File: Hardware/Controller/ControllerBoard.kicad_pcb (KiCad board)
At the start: 2 copper layers, 25 x 140 mm, 31 parts, among them J1 Conn_01x08_MountingPin, J2 USB4715-GF-A_REVA, Q1 BC818, Q2 AO3401A, Q3 BC818, X1 CON_JST_PH_2PIN_MTPH2, X2 CON_JST_PH_2PIN_MTPH2

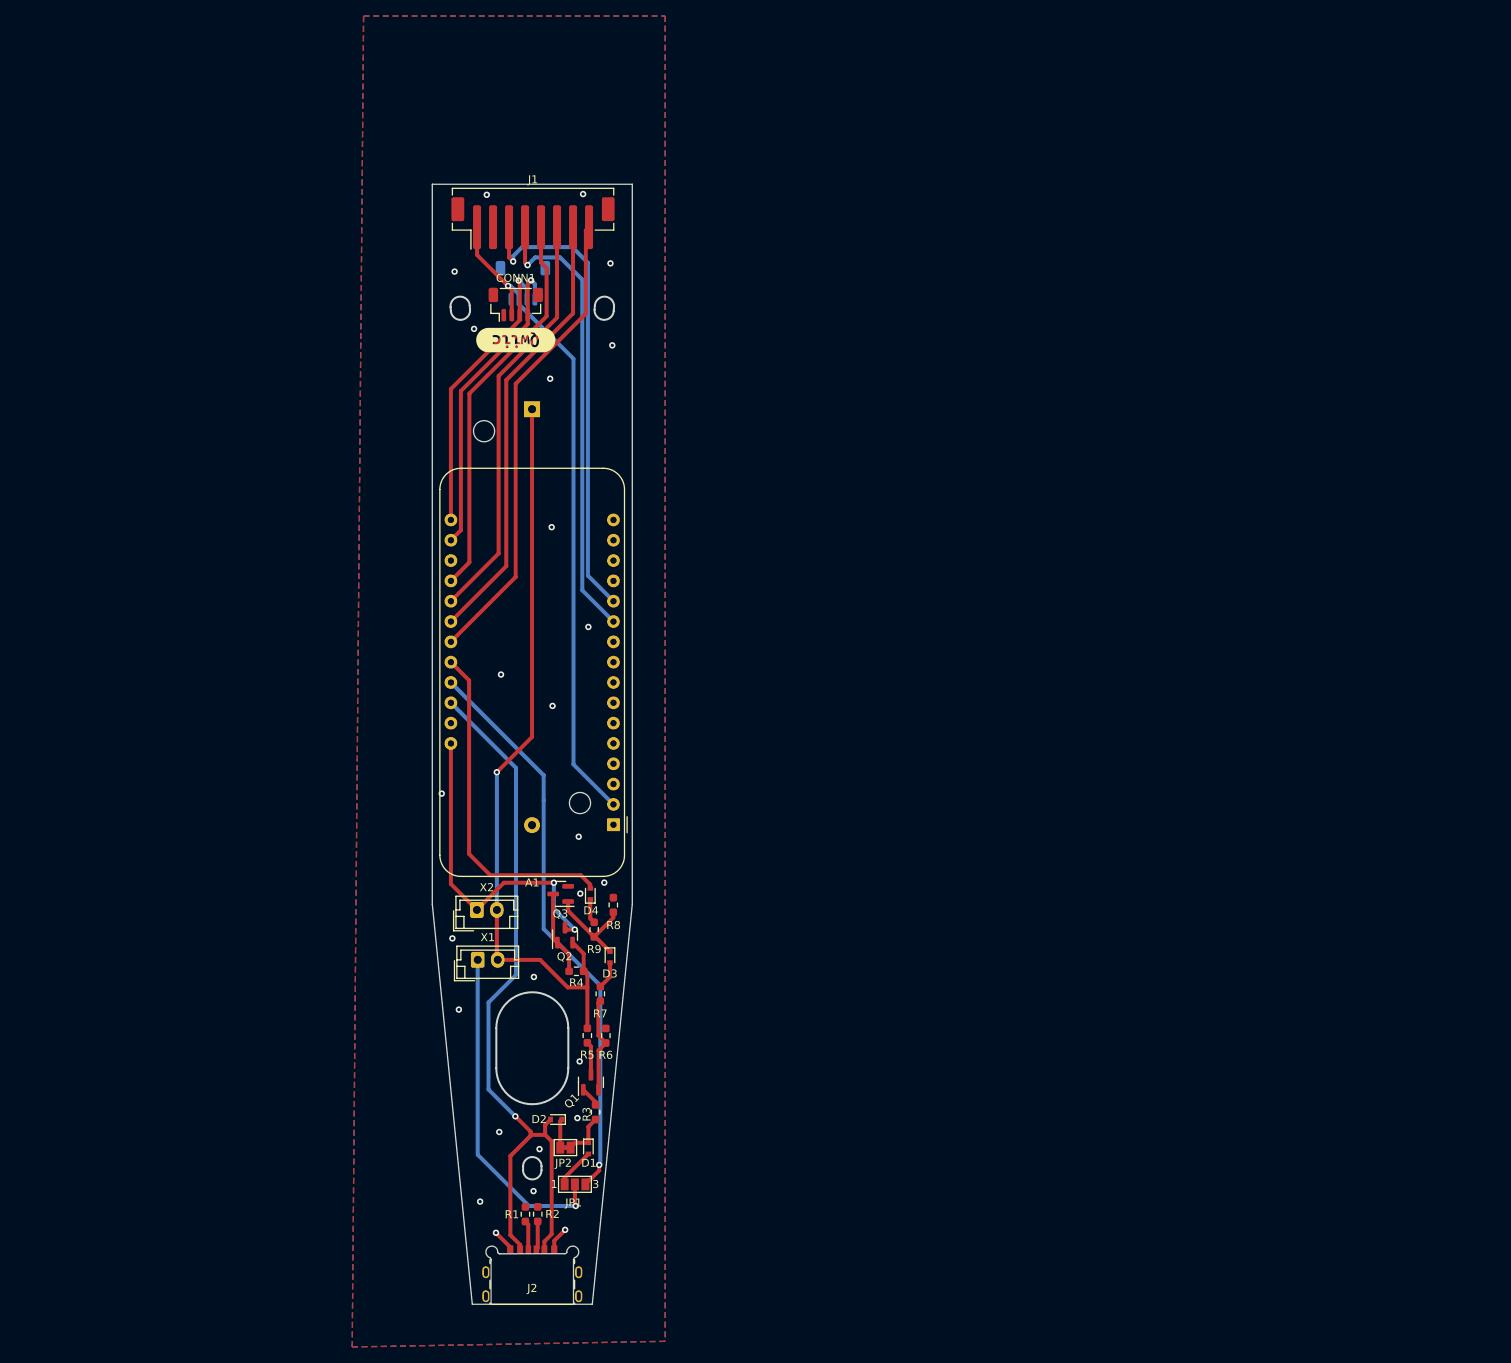
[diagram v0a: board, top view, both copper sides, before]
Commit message: Initial conversion and cleanup from a feather to an esp32s3
added USB power
Added switching 3.6-5v regulator
updated schematic ground to use built in kicad libraries
updated partially broken library references to eagle lib files
added circuit simulator of trigger and wakeup simulation

Signed-off-by: lokimetasmith <lokimail@gmail.com>
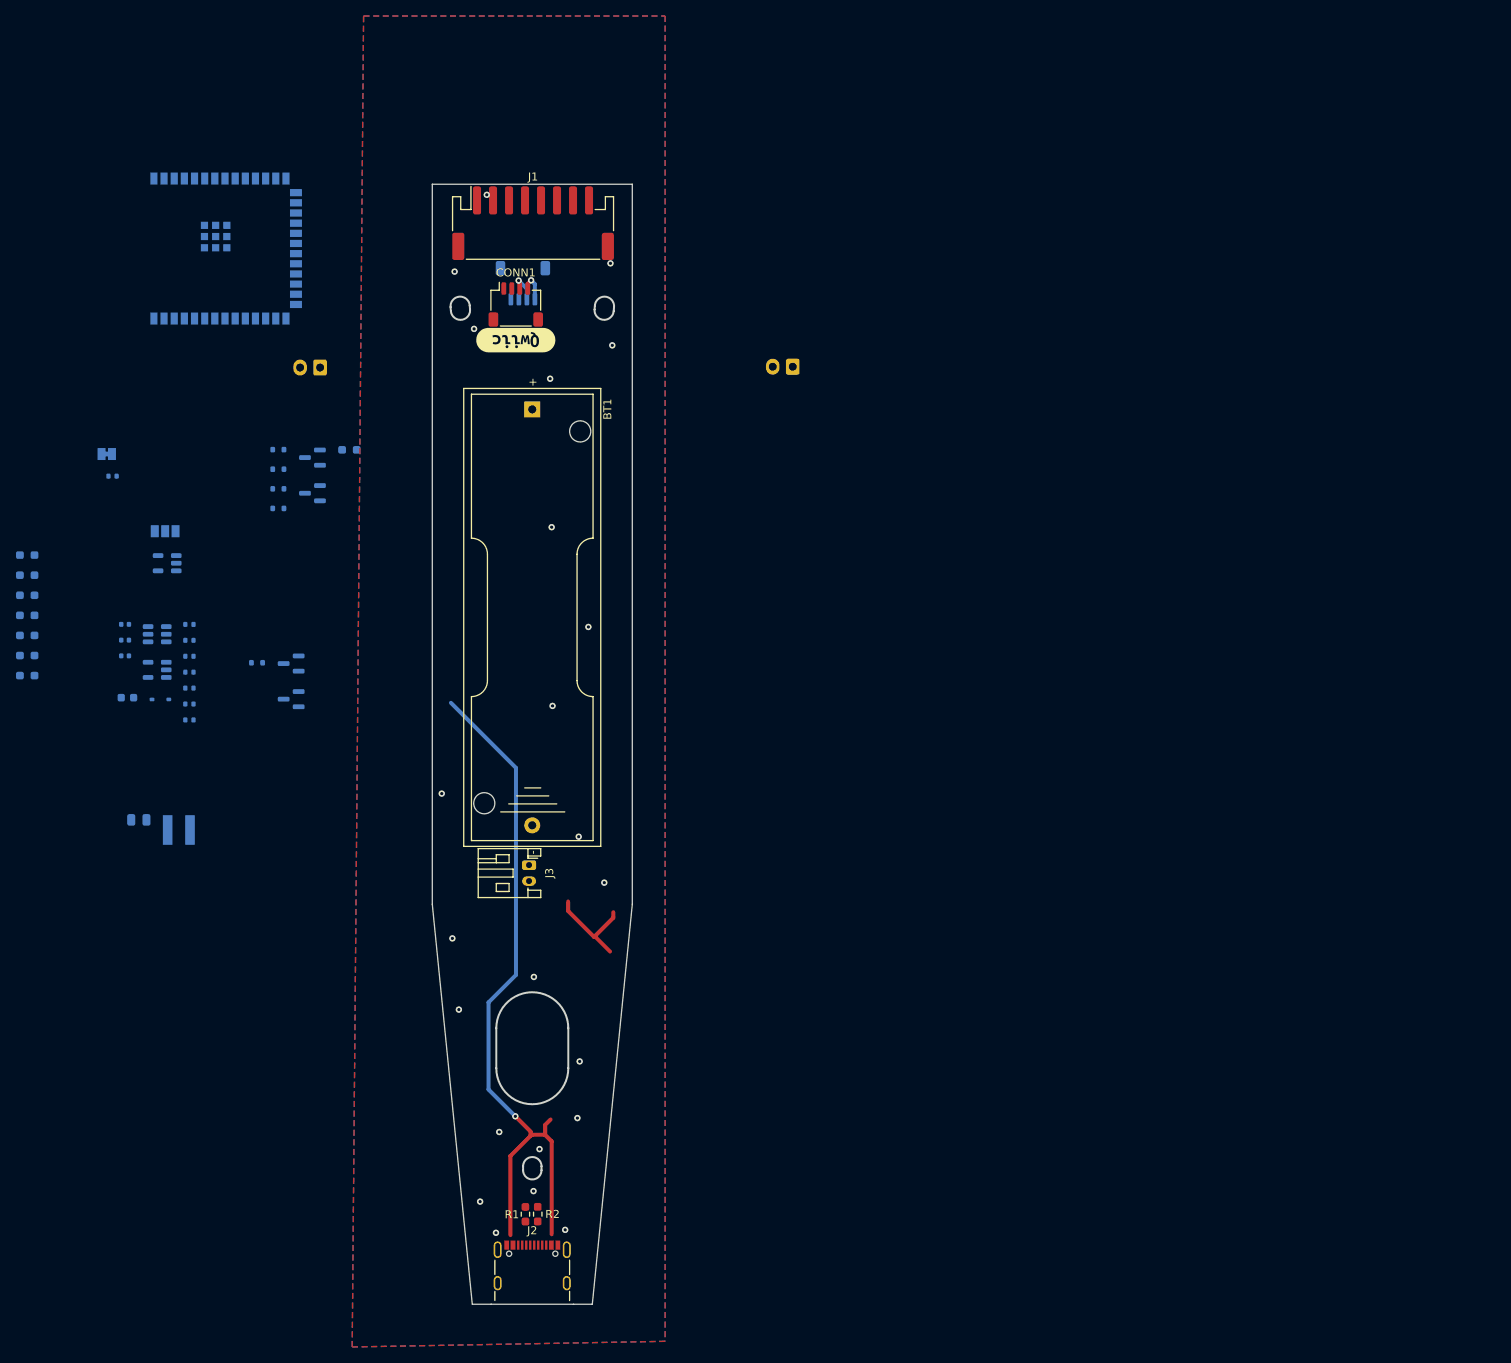
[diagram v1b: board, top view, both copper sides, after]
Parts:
- removed A1: Adafruit_Feather_HUZZAH32_ESP32, Module:Adafruit_Feather
- added C1: 2u, Capacitor_SMD:C_0603_1608Metric, B.Cu at (60.0, 99.2)
- added C2: 4.7u, Capacitor_SMD:C_0805_2012Metric, B.Cu at (61.5, 114.5)
- added C5: 6.8p, Capacitor_SMD:C_0402_1005Metric, B.Cu at (59.7, 90.0)
- added C6: 0.01u, Capacitor_SMD:C_0402_1005Metric, B.Cu at (59.7, 92.0)
- added C8: 0.1u, Capacitor_SMD:C_0402_1005Metric, B.Cu at (59.7, 94.0)
- added D5: 3.3v_TVS, Diode_SMD:D_SOD-323, B.Cu at (64.2, 99.4)
- added D6: BAS516, Diode_SMD:D_SOD-523, B.Cu at (76.2, 94.8)
- added J3: Conn_01x02_Male, Connector_JST:JST_PH_S2B-PH-K_1x02_P2.00mm_Horizontal, F.Cu at (110.2, 120.1)
- added L1: 2.2uH, Inductor_SMD:L_Taiyo-Yuden_MD-4040, B.Cu at (66.5, 115.7)
- added Q4: AO3401A, Package_TO_SOT_SMD:SOT-23, B.Cu at (80.5, 99.4)
- added R10: 15K, Resistor_SMD:R_0402_1005Metric, B.Cu at (67.8, 90.0)
- added R11: 15K, Resistor_SMD:R_0402_1005Metric, B.Cu at (67.8, 92.0)
- added R12: 27, Resistor_SMD:R_0402_1005Metric, B.Cu at (67.8, 94.0)
- added R13: 27, Resistor_SMD:R_0402_1005Metric, B.Cu at (67.8, 96.0)
- added R14: 10K, Resistor_SMD:R_0402_1005Metric, B.Cu at (67.8, 98.0)
- added R15: 680k, Resistor_SMD:R_0402_1005Metric, B.Cu at (67.8, 100.0)
- added R16: 150K, Resistor_SMD:R_0402_1005Metric, B.Cu at (67.8, 102.0)
- added R17: 5.1k, Resistor_SMD:R_0402_1005Metric, B.Cu at (58.2, 71.5)
- added R18: 100k, Resistor_SMD:R_0603_1608Metric_Pad0.98x0.95mm_HandSolder, B.Cu at (47.5, 96.4)
- added U1: ESP32-S3-WROOM-1, Espressif:ESP32-S3-WROOM-1, B.Cu at (71.6, 43.0)
- added U2: SN65220, Package_TO_SOT_SMD:SOT-23-6, B.Cu at (63.8, 91.3)
- added U3: TLV62569DBV, Package_TO_SOT_SMD:SOT-23-5, B.Cu at (63.8, 95.7)
- added U5: MCP73811T-420I-OT, Package_TO_SOT_SMD:SOT-23-5, B.Cu at (65.0, 82.4)
- BT1: moved to F.Cu
- CONN1: footprint Connector_JST:JST_SH_BM04B-SRSS-TB_1x04-1MP_P1.00mm_Vertical -> Connector_JST:JST_SH_SM04B-SRSS-TB_1x04-1MP_P1.00mm_Horizontal
- D1, D2, D3, D4, JP1, JP2, Q1, Q2, Q3, R3, R4, R5, R6, R7, R8, R9, X1, X2: moved to B.Cu
- J1: footprint Connector_JST:JST_PH_B8B-PH-SM4-TB_1x08-1MP_P2.00mm_Vertical -> Connector_JST:JST_PH_S8B-PH-SM4-TB_1x08-1MP_P2.00mm_Horizontal
- J2: value USB4715-GF-A_REVA -> USB_C_Receptacle_USB2.0; footprint USB4715-GF-A_REVA:GCT_USB4715-GF-A_REVA -> Connector_USB:USB_C_Receptacle_GCT_USB4105-xx-A_16P_TopMnt_Horizontal
- moved JP2 103.9 mm to (57.5, 68.7), turned to 180 degrees
- moved JP1 96.4 mm to (64.8, 78.4), turned to 180 degrees
- moved D1 95.6 mm to (78.9, 68.2), turned to 180 degrees
- moved R6 90.9 mm to (47.5, 86.4), turned to 180 degrees
- moved R5 90.6 mm to (47.5, 83.9), turned to 180 degrees
- moved D2 88.4 mm to (78.9, 70.6)
- moved R3 88.3 mm to (87.8, 68.2), turned to 180 degrees
- moved R4 86.1 mm to (47.5, 81.4)
- moved R7 85.9 mm to (47.5, 88.9), turned to 180 degrees
- moved Q1 85.5 mm to (83.2, 69.2), turned to 180 degrees
- moved X1 83.9 mm to (143.2, 57.8), turned to 180 degrees
- moved R8 80.6 mm to (47.5, 91.4), turned to 180 degrees
- moved R9 78.7 mm to (47.5, 93.9), turned to 180 degrees
- moved D3 71.7 mm to (78.9, 73.1), turned to 180 degrees
- moved X2 70.6 mm to (84.1, 57.9), turned to 180 degrees
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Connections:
- net Net-(A1-Pad17) renamed /SDA
- net Net-(A1-Pad18) renamed /SCL
- net Net-(BT1-Pad1) renamed /Trigger_Wake_Up/VBAT
- net power for the esp32 renamed Net-(Q2-D)
- D4 pad 2: KeepAlive -> /KeepAlive
- J1 pad 3: Net-(A1-Pad12) -> /GPIO18/MOSI
- J1 pad 4: Net-(A1-Pad11) -> /GPIO5/SCK
- J1 pad 5: Net-(A1-Pad20) -> /GPIO32
- J1 pad 6: Net-(A1-Pad21) -> /GPIO15
- J1 pad 7: Net-(A1-Pad22) -> /GPIO33
- J1 pad 8: Net-(A1-Pad23) -> /GPIO27
- J2 pad A12: GND -> Net-(J2-GND-PadA1)
- J2 pad A5: Net-(J2-PadA5) -> Net-(J2-CC1)
- J2 pad B12: GND -> Net-(J2-GND-PadA1)
- J2 pad B5: Net-(J2-PadB5) -> Net-(J2-CC2)
- J2 pad S1: Net-(J2-PadS1) -> /Shield
- JP1 pad 3: Trigger -> /Trigger
- Q3 pad 2: GND -> unconnected-(Q3-E-Pad2)
- R1 pad 1: Net-(J2-PadA5) -> Net-(J2-CC2)
- R2 pad 1: GND -> Net-(J2-CC1)
- R2 pad 2: Net-(J2-PadB5) -> GND
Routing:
- net GND: track 5.88 -> 104.0 mm, vias 26 -> 24
- net USB_pwr: track 96.0 -> 0.00 mm, vias 1 -> 0
- net /Trigger_Wake_Up/VBAT: track 94.8 -> 0.00 mm, vias 1 -> 0
- net 3.3V: track 83.2 -> 0.00 mm, vias 1 -> 0
- net Trigger: track 71.2 -> 0.00 mm, vias 1 -> 0
- net Net-(A1-Pad12): track 59.4 -> 0.00 mm, vias 1 -> 0
- net Net-(A1-Pad23): track 59.0 -> 0.00 mm
- net Net-(A1-Pad11): track 57.6 -> 0.00 mm, vias 1 -> 0
- net Net-(A1-Pad22): track 55.6 -> 0.00 mm
- net Net-(A1-Pad21): track 52.2 -> 0.00 mm
- net Net-(A1-Pad20): track 49.5 -> 0.00 mm
- net KeepAlive: track 42.1 -> 0.00 mm
- net Net-(JP1-C): track 42.0 -> 0.00 mm, vias 1 -> 0
- net Net-(Q2-D): track 41.5 -> 0.00 mm, vias 2 -> 0
- net /SCL: track 39.2 -> 3.14 mm
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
